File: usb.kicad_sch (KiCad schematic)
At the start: 27 parts, among them J2 USB4105, J3 USB1130, U1 MX6UL-VM, U11 TPD4EUSB30, U12 74LVC1G06, U13 D5V0H1B2LP, U4 TUSB320, U5 AP22814AW5, U6 TPD4EUSB30, U7 D5V0H1B2LP

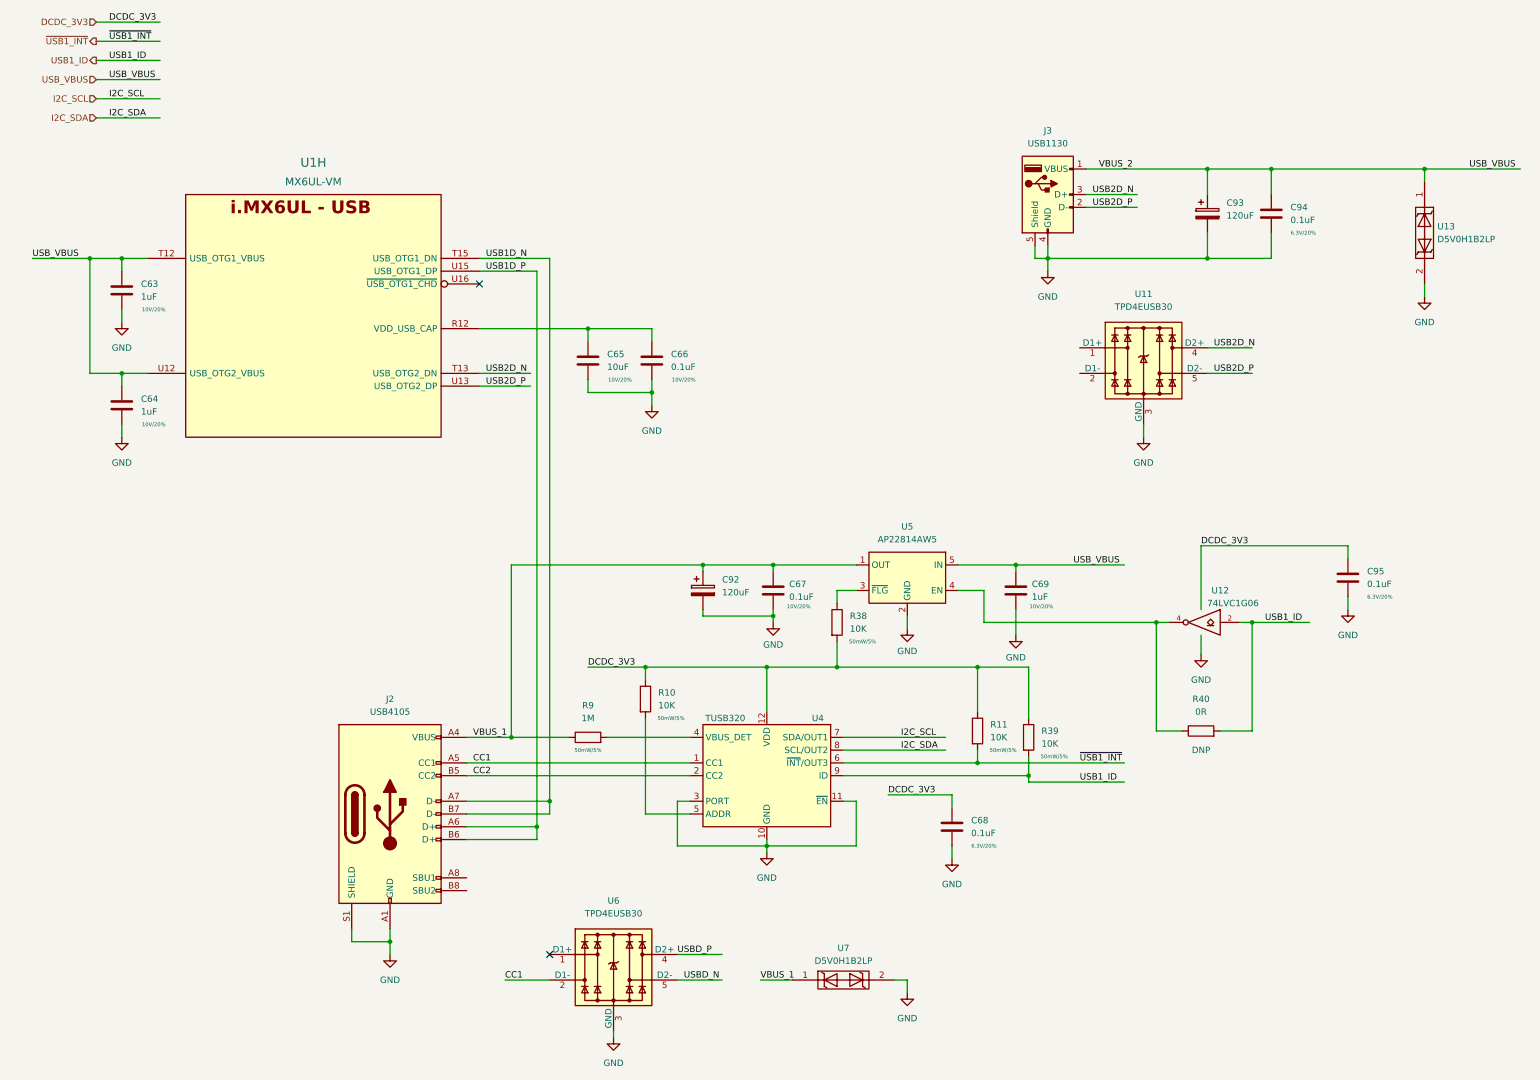
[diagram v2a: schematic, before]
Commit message: move to hierarchal labels, work on power tree, add basic pcb layout
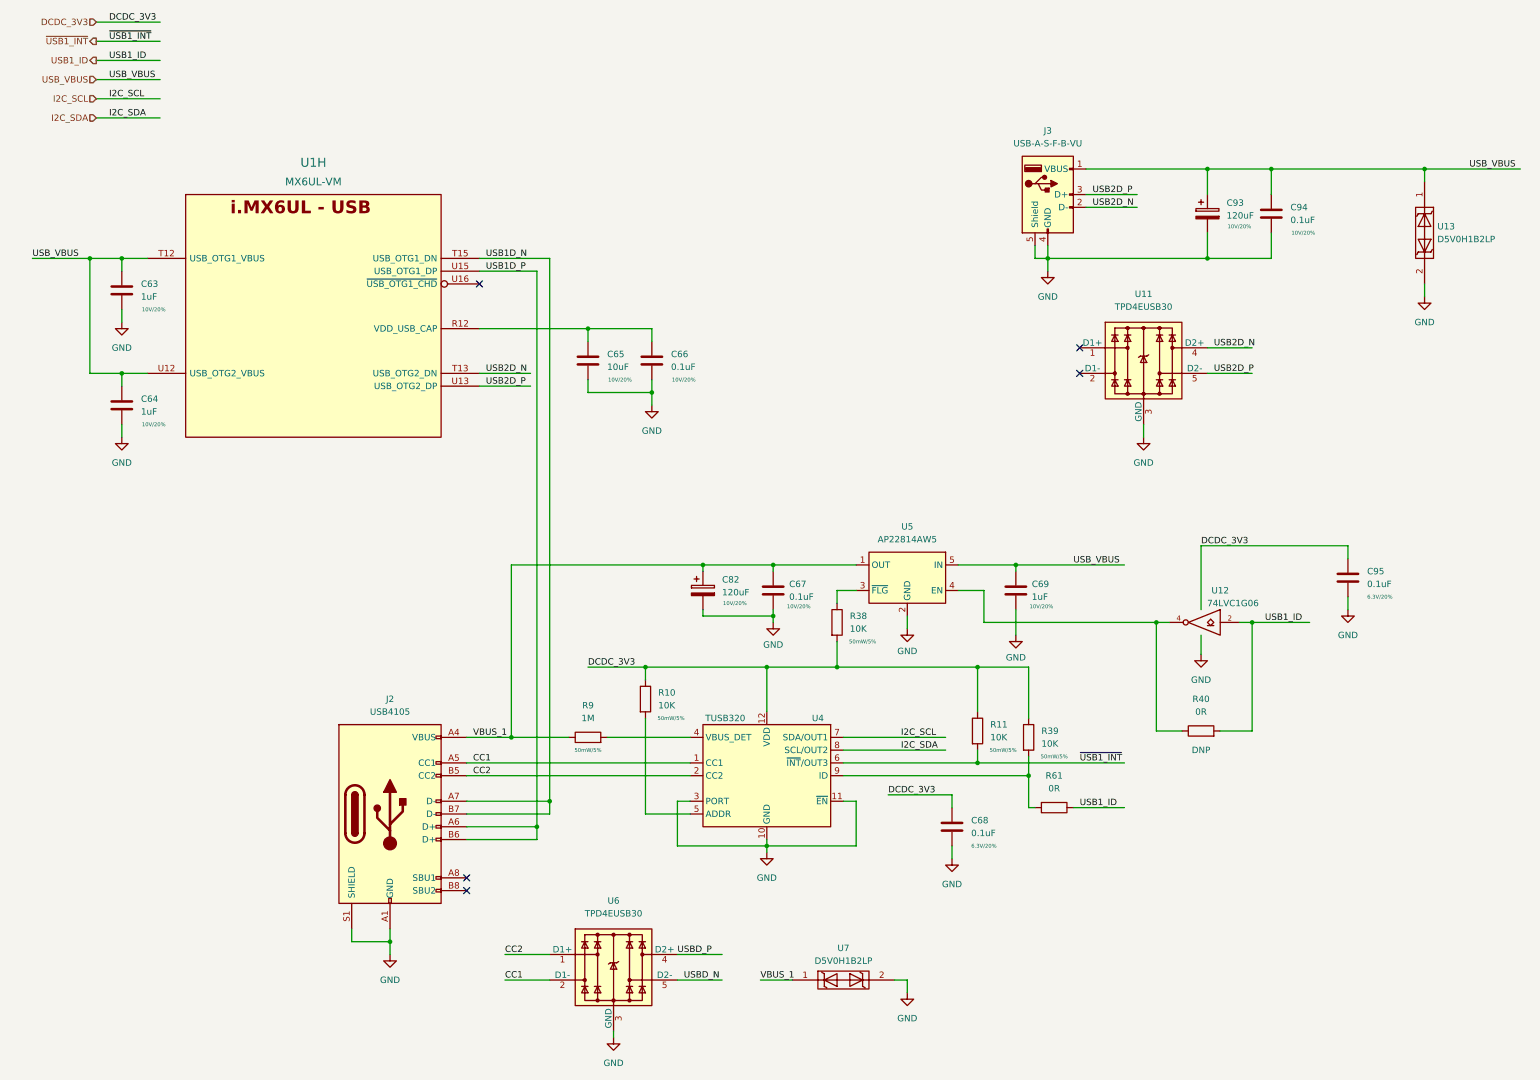
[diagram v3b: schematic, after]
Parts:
- removed C92: 120uF, Capacitor_SMD:CP_Elec_5x5.8, symbol Device:C_Polarized
- added C82: 120uF, Capacitor_SMD:CP_Elec_5x5.8, symbol Device:C_Polarized
- added R61: 0R, Resistor_SMD:R_0402_1005Metric, symbol Device:R
- C93: Rating (none) -> 10V/20%
- C94: Rating 6.3V/20% -> 10V/20%
- J3: value USB1130 -> USB-A-S-F-B-VU; footprint imx6ull-sbc:GCT_USB1130-15-A_REVA -> imx6ull-sbc:SAMTEC_USB-A-S-X-X-VU
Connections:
- net CC2: now also U6.1 (D1+), U6.10
- net GND: now also C82.2
- net USB1_ID: now also R61.1; no longer R39.2, U4.9 (ID)
- net USB2D_N: now also J3.2 (D-); no longer J3.3 (D+)
- net USB2D_P: now also J3.3 (D+); no longer J3.2 (D-)
- net VBUS_1: now also C82.1
- new net: R39.2, R61.2, U4.9 (ID)
- no-connect marks 2 -> 5
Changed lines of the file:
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@@
   (junction (at 153.67 127) (diameter 0) (color 0 0 0 0)
   )
-  (no_connect (at 123.19 204.47))
+  (no_connect (at 228.6 88.9))
+  (no_connect (at 228.6 83.82))
   (no_connect (at 109.22 71.12))
+  (no_connect (at 106.68 189.23))
+  (no_connect (at 106.68 191.77))
   (wire (pts (xy 190.5 172.72) (xy 203.2 172.72))
     (stroke (width 0) (type default) (color 0 0 0 0))
@@
     (stroke (width 0) (type default) (color 0 0 0 0))
   )
-  (wire (pts (xy 218.44 170.18) (xy 218.44 168.91))
+  (wire (pts (xy 218.44 168.91) (xy 218.44 175.26))
     (stroke (width 0) (type default) (color 0 0 0 0))
   )
@@
     (stroke (width 0) (type default) (color 0 0 0 0))
   )
-  (wire (pts (xy 218.44 170.18) (xy 237.49 170.18))
-    (stroke (width 0) (type default) (color 0 0 0 0))
-  )
   (wire (pts (xy 167.64 137.16) (xy 167.64 138.43))
     (stroke (width 0) (type default) (color 0 0 0 0))
@@
     (stroke (width 0) (type default) (color 0 0 0 0))
   )
+  (wire (pts (xy 218.44 175.26) (xy 219.71 175.26))
+    (stroke (width 0) (type default) (color 0 0 0 0))
+  )
   (wire (pts (xy 123.19 176.53) (xy 106.68 176.53))
     (stroke (width 0) (type default) (color 0 0 0 0))
@@
     (stroke (width 0) (type default) (color 0 0 0 0))
   )
+  (wire (pts (xy 114.3 204.47) (xy 123.19 204.47))
+    (stroke (width 0) (type default) (color 0 0 0 0))
+  )
   (wire (pts (xy 297.18 71.12) (xy 297.18 73.66))
     (stroke (width 0) (type default) (color 0 0 0 0))
@@
     (stroke (width 0) (type default) (color 0 0 0 0))
   )
+  (wire (pts (xy 227.33 175.26) (xy 237.49 175.26))
+    (stroke (width 0) (type default) (color 0 0 0 0))
+  )
   (wire (pts (xy 91.44 201.93) (xy 91.44 204.47))
     (stroke (width 0) (type default) (color 0 0 0 0))
@@
     (effects (font (size 1.27 1.27)) (justify left bottom))
   )
-  (label "USB2D_P" (at 231.14 55.88 0)
-    (effects (font (size 1.27 1.27)) (justify left bottom))
-  )
-  (label "USB2D_N" (at 231.14 53.34 0)
+  (label "CC2" (at 114.3 204.47 0)
+    (effects (font (size 1.27 1.27)) (justify left bottom))
+  )
+  (label "USB2D_P" (at 231.14 53.34 0)
+    (effects (font (size 1.27 1.27)) (justify left bottom))
+  )
+  (label "USB2D_N" (at 231.14 55.88 0)
     (effects (font (size 1.27 1.27)) (justify left bottom))
   )
@@
     (effects (font (size 1.27 1.27)) (justify left bottom))
   )
-  (label "VBUS_2" (at 232.41 48.26 0)
-    (effects (font (size 1.27 1.27)) (justify left bottom))
-  )
   (label "VBUS_1" (at 107.95 161.29 0)
     (effects (font (size 1.27 1.27)) (justify left bottom))
@@
     (effects (font (size 1.27 1.27)) (justify left bottom))
   )
-  (label "USB1_ID" (at 228.6 170.18 0)
+  (label "USB1_ID" (at 228.6 175.26 0)
     (effects (font (size 1.27 1.27)) (justify left bottom))
   )
@@
   )
   (symbol (lib_id "Device:C_Polarized") (at 254 57.15 0) (unit 1)
-    (in_bom yes) (on_board yes) (fields_autoplaced)
+    (in_bom yes) (on_board yes)
     (property "Reference" "C93" (id 0) (at 257.81 54.9909 0)
       (effects (font (size 1.27 1.27)) (justify left))
@@
     (property "Datasheet" "~" (id 3) (at 254 57.15 0)
       (effects (font (size 1.27 1.27)) hide)
+    )
+    (property "Rating" "10V/20%" (id 4) (at 260.35 59.69 0)
+      (effects (font (size 0.762 0.762)))
     )
     (pin "1")
@@
     )
     (pin "1")
+  )
+  (symbol (lib_id "Device:R") (at 223.52 175.26 270) (unit 1)
+    (in_bom yes) (on_board yes) (fields_autoplaced)
+    (property "Reference" "R61" (id 0) (at 223.52 168.91 90))
+    (property "Value" "0R" (id 1) (at 223.52 171.45 90))
+    (property "Footprint" "Resistor_SMD:R_0402_1005Metric" (id 2) (at 223.52 173.482 90)
+      (effects (font (size 1.27 1.27)) hide)
+    )
+    (property "Datasheet" "~" (id 3) (at 223.52 175.26 0)
+      (effects (font (size 1.27 1.27)) hide)
+    )
+    (pin "1")
+    (pin "2")
   )
   (symbol (lib_id "power:GND") (at 38.1 78.74 0) (unit 1)
@@
       (effects (font (size 1.27 1.27)) hide)
     )
-    (property "Rating" "6.3V/20%" (id 4) (at 273.05 60.96 0)
+    (property "Rating" "10V/20%" (id 4) (at 273.05 60.96 0)
       (effects (font (size 0.762 0.762)))
     )
@@
     (pin "1")
   )
+  (symbol (lib_id "Device:C_Polarized") (at 153.67 132.08 0) (unit 1)
+    (in_bom yes) (on_board yes)
+    (property "Reference" "C82" (id 0) (at 157.48 129.9209 0)
+      (effects (font (size 1.27 1.27)) (justify left))
+    )
+    (property "Value" "120uF" (id 1) (at 157.48 132.4609 0)
+      (effects (font (size 1.27 1.27)) (justify left))
+    )
+    (property "Footprint" "Capacitor_SMD:CP_Elec_5x5.8" (id 2) (at 154.6352 135.89 0)
+      (effects (font (size 1.27 1.27)) hide)
+    )
+    (property "Datasheet" "~" (id 3) (at 153.67 132.08 0)
+      (effects (font (size 1.27 1.27)) hide)
+    )
+    (property "Rating" "10V/20%" (id 4) (at 160.02 134.62 0)
+      (effects (font (size 0.762 0.762)))
+    )
+    (pin "1")
+    (pin "2")
+  )
   (symbol (lib_id "power:GND") (at 167.64 138.43 0) (unit 1)
     (in_bom yes) (on_board yes) (fields_autoplaced)
@@
     )
     (pin "1")
-  )
-  (symbol (lib_id "Device:C_Polarized") (at 153.67 132.08 0) (unit 1)
-    (in_bom yes) (on_board yes) (fields_autoplaced)
-    (property "Reference" "C92" (id 0) (at 157.48 129.9209 0)
-      (effects (font (size 1.27 1.27)) (justify left))
-    )
-    (property "Value" "120uF" (id 1) (at 157.48 132.4609 0)
-      (effects (font (size 1.27 1.27)) (justify left))
-    )
-    (property "Footprint" "Capacitor_SMD:CP_Elec_5x5.8" (id 2) (at 154.6352 135.89 0)
-      (effects (font (size 1.27 1.27)) hide)
-    )
-    (property "Datasheet" "~" (id 3) (at 153.67 132.08 0)
-      (effects (font (size 1.27 1.27)) hide)
-    )
-    (pin "1")
-    (pin "2")
   )
   (symbol (lib_id "Device:R") (at 180.34 138.43 0) (unit 1)
@@
     (in_bom yes) (on_board yes) (fields_autoplaced)
     (property "Reference" "J3" (id 0) (at 222.25 40.64 0))
-    (property "Value" "USB1130" (id 1) (at 222.25 43.18 0))
-    (property "Footprint" "imx6ull-sbc:GCT_USB1130-15-A_REVA" (id 2) (at 226.06 54.61 0)
-      (effects (font (size 1.27 1.27)) hide)
-    )
+    (property "Value" "USB-A-S-F-B-VU" (id 1) (at 222.25 43.18 0))
+    (property "Footprint" "imx6ull-sbc:SAMTEC_USB-A-S-X-X-VU" (id 2) (at 226.06 54.61 0)
+      (effects (font (size 1.27 1.27)) hide)
+    )

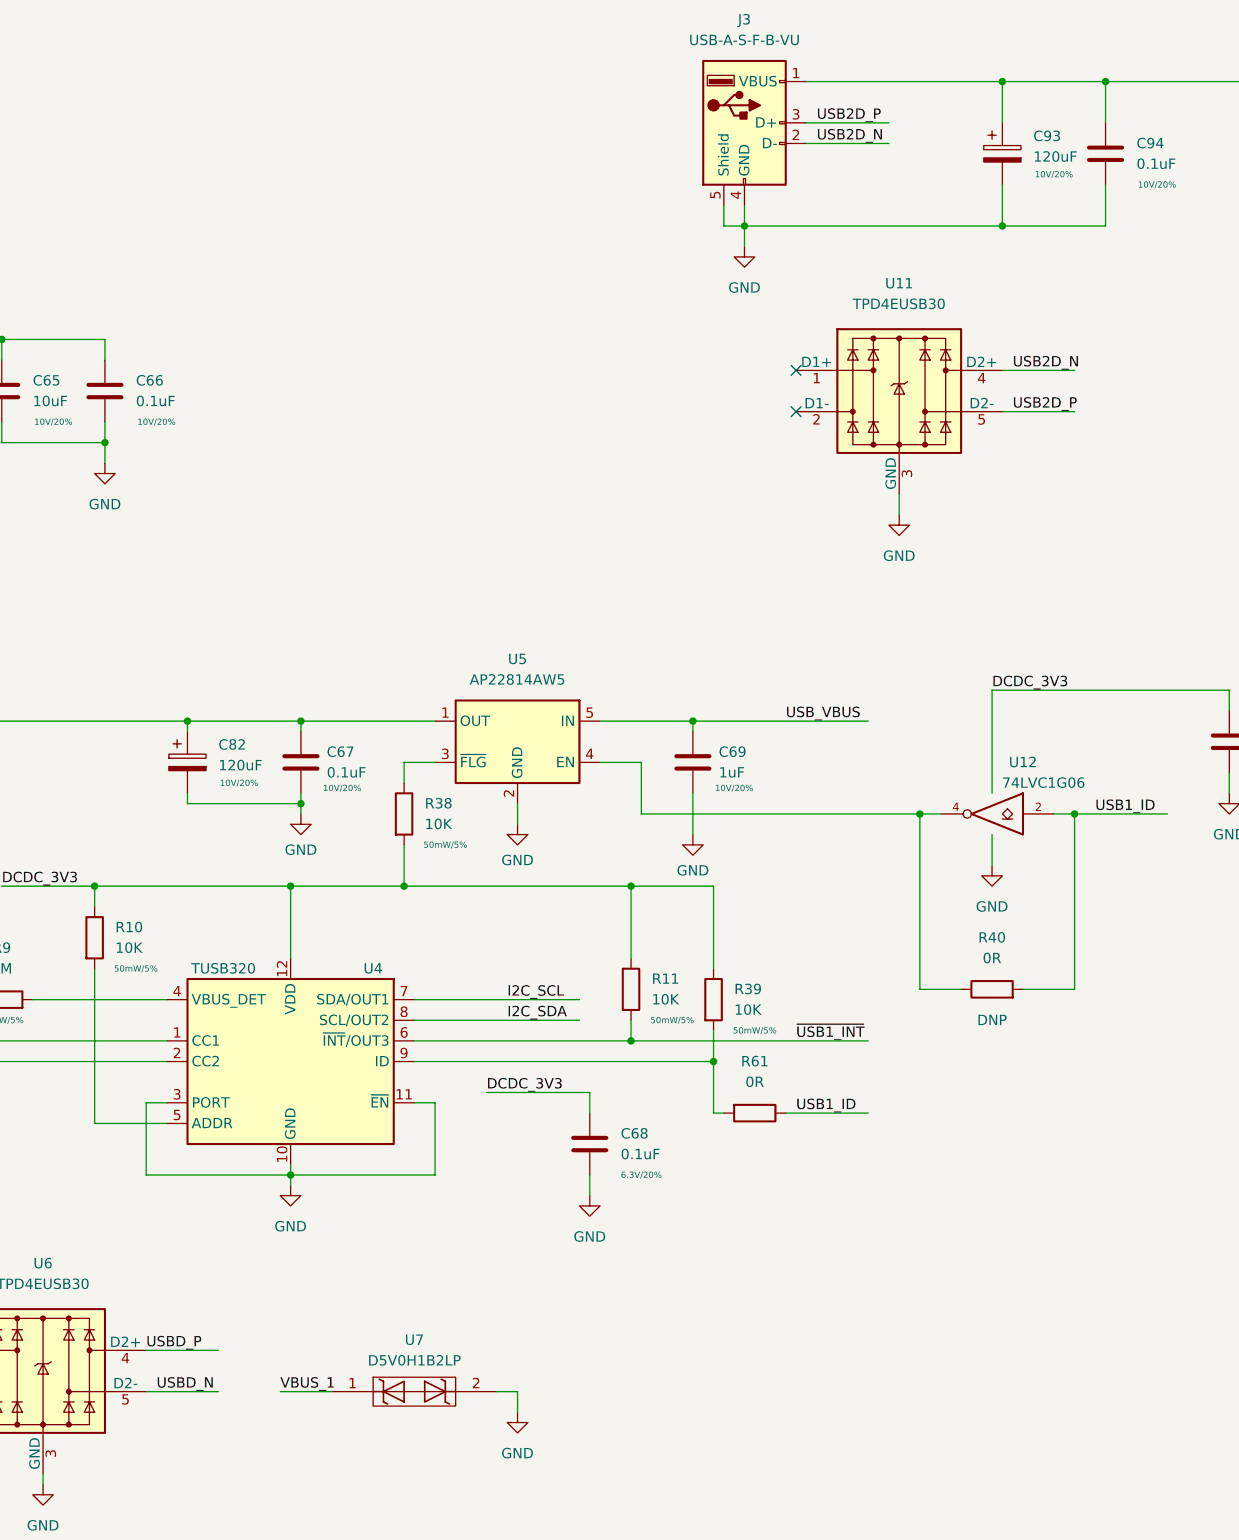
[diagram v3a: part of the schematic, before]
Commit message: most of sch done, inital component pcb placement
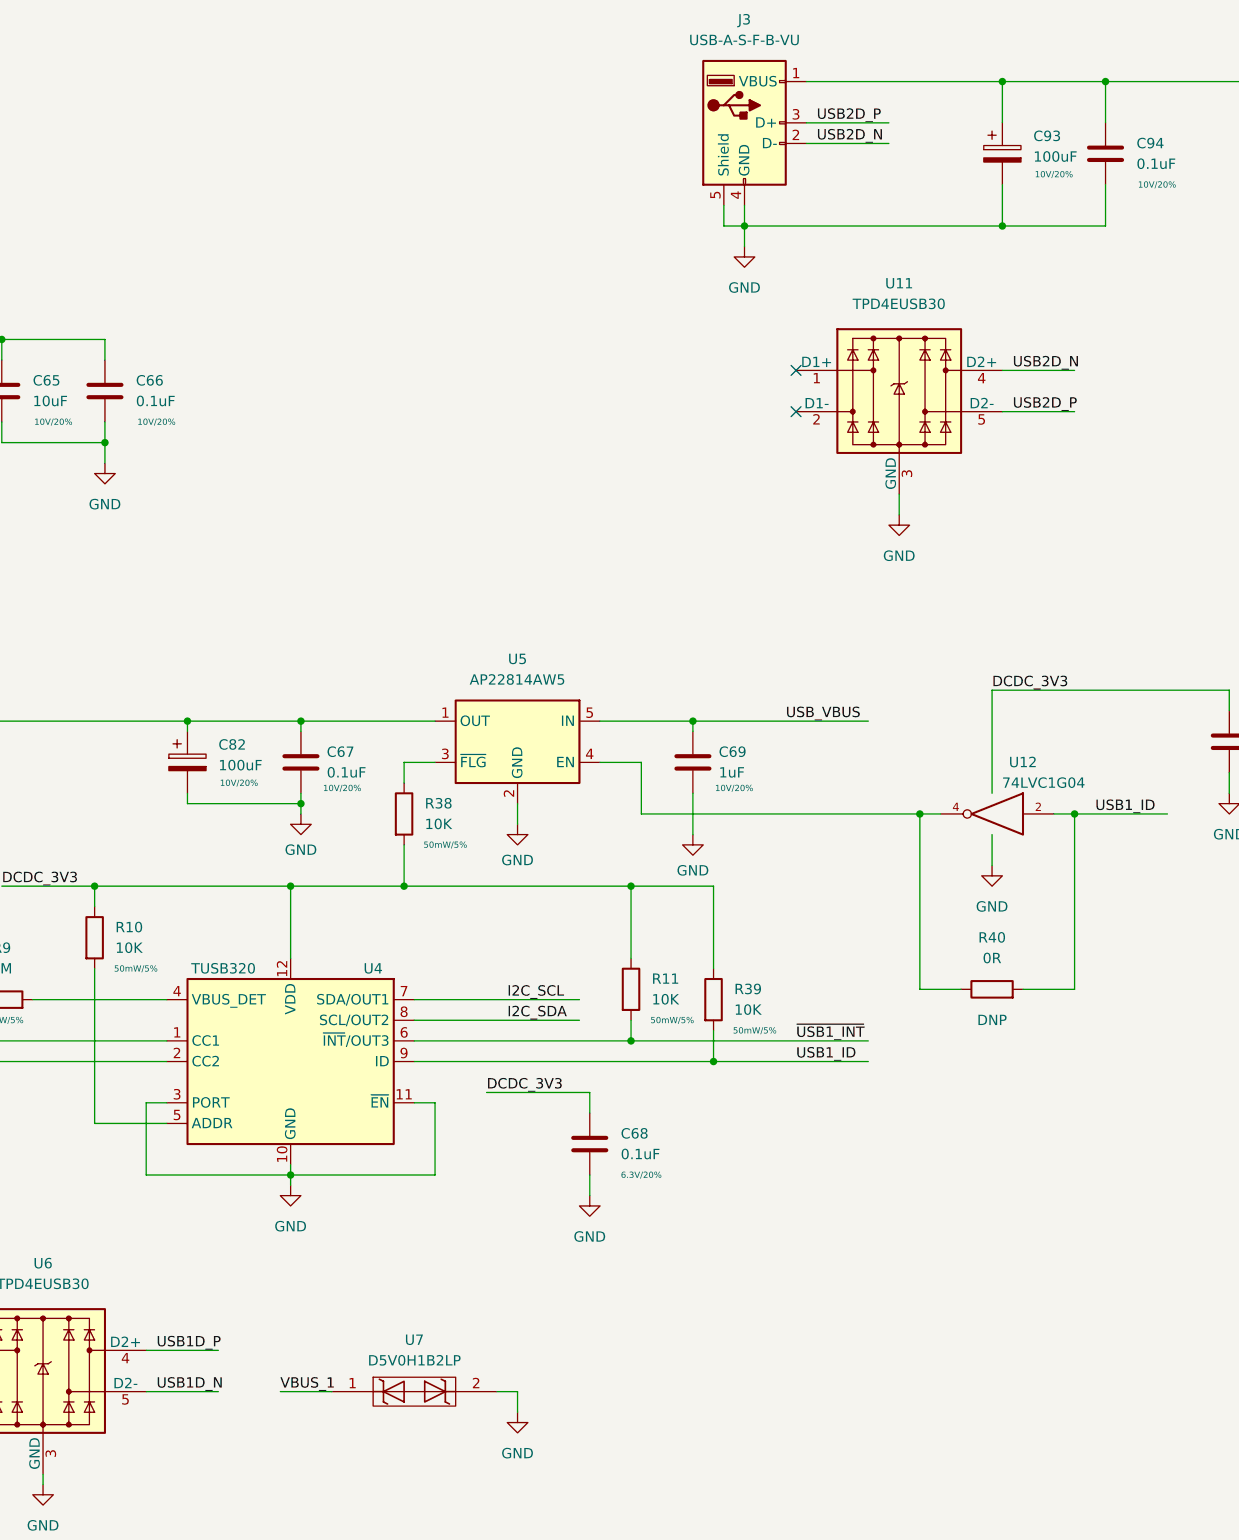
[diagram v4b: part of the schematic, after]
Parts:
- removed R61: 0R, Resistor_SMD:R_0402_1005Metric, symbol Device:R
- removed U12: 74LVC1G06, Package_TO_SOT_SMD:SOT-23-5, symbol 74xGxx:74LVC1G06
- added U12: 74LVC1G04, Package_TO_SOT_SMD:SOT-23-5, symbol 74xGxx:74LVC1G04
- C82, C93: value 120uF -> 100uF; footprint Capacitor_SMD:CP_Elec_5x5.8 -> Capacitor_Tantalum_SMD:CP_EIA-3528-15_AVX-H
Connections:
- net USBD_N is gone; now on net USB1D_N: U6.5 (D2-), U6.6
- net USBD_P is gone; now on net USB1D_P: U6.4 (D2+), U6.7
- net GND: now also U12.3 (GND)
- net USB1_ID: now also R39.2, U4.9 (ID), U12.2
- net VCC: now also U12.5 (VCC)
- net at R40.1, U5.4 (EN): now also U12.4
